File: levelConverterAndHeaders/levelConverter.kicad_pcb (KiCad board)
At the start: 2 copper layers, 30 parts, among them J1 S, J2 Term, J3 S, J4 Term, Q1 BSS138, Q2 BSS138, Q3 BSS138, Q4 BSS138, Q5 BSS138, Q6 BSS138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

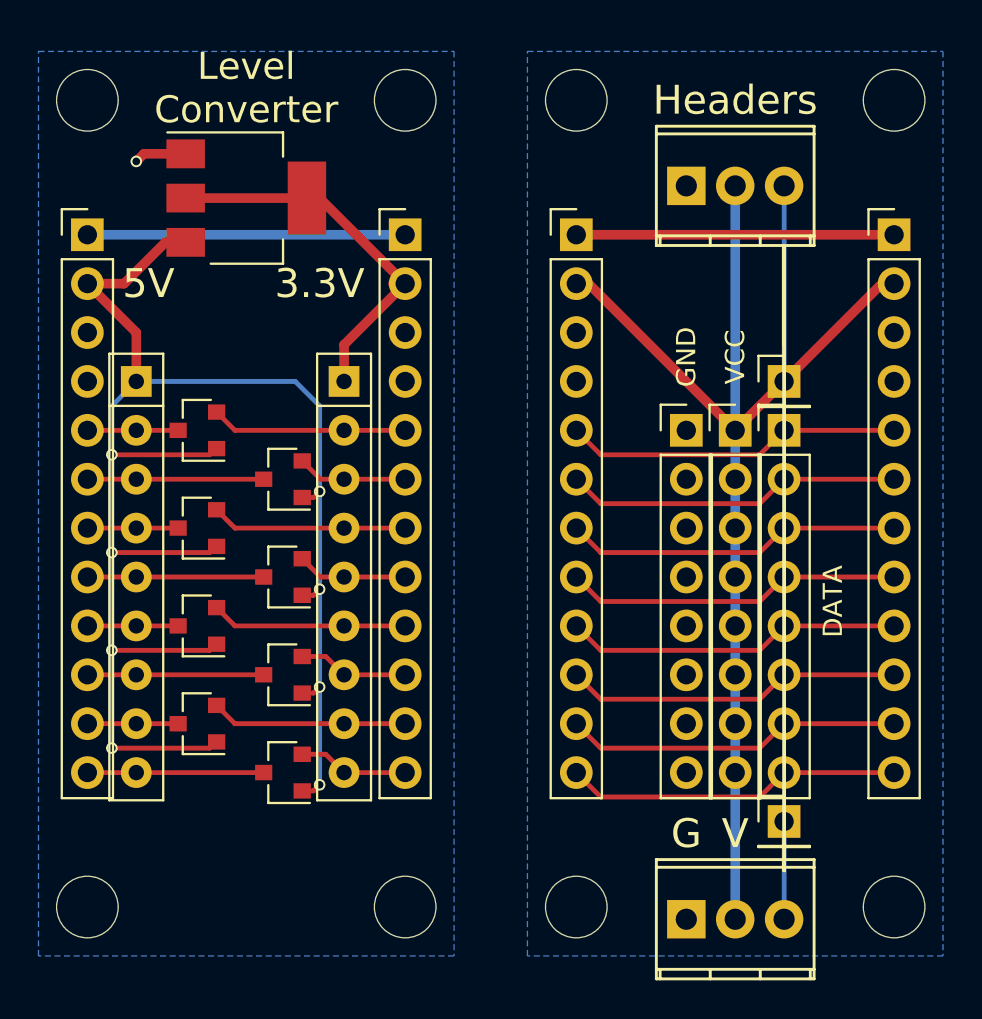
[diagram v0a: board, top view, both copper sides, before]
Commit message: More work to ensure there are no errors from KiCAD's schematic checker. Fixed the multiplexer module, so that all 7 slaves will work (only 6 were working, due to a missing VCC to the "Next Output").
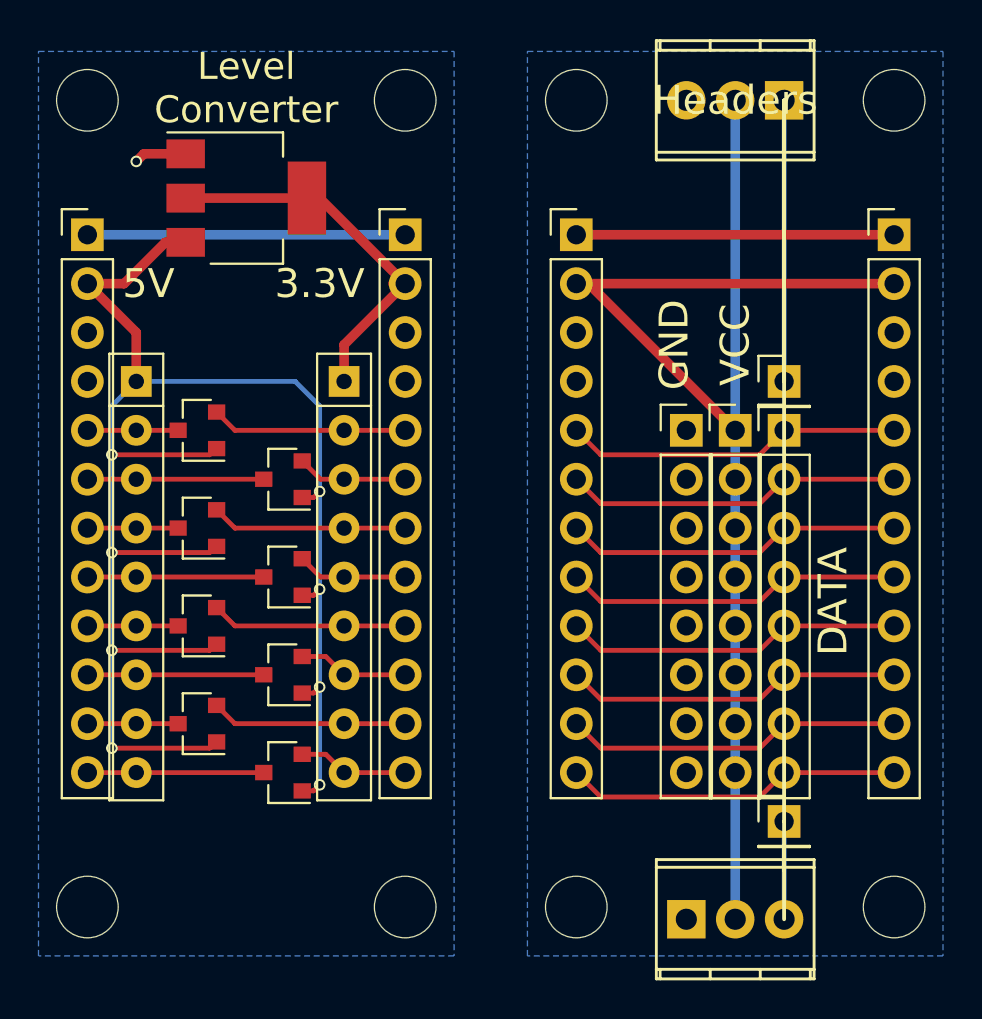
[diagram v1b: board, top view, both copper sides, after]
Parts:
- removed H1: DATA, Pin_Headers:Pin_Header_Straight_1x08_Pitch2.54mm
- removed H2: GND, Pin_Headers:Pin_Header_Straight_1x08_Pitch2.54mm
- removed H3: VCC, Pin_Headers:Pin_Header_Straight_1x08_Pitch2.54mm
- added J5: GND, Pin_Headers:Pin_Header_Straight_1x08_Pitch2.54mm, F.Cu at (159.4, 103.5)
- added J6: VCC, Pin_Headers:Pin_Header_Straight_1x08_Pitch2.54mm, F.Cu at (161.9, 103.5)
- added J7: Data, Pin_Headers:Pin_Header_Straight_1x08_Pitch2.54mm, F.Cu at (164.5, 103.5)
- moved J4 6.75 mm to (164.5, 86.4), turned to 180 degrees
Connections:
- net Net-(H3-Pad1) renamed /VCC2
- I1 pad 3: Earth -> /GND
- I2 pad 3: Earth -> /GND2
- J2 pad 1: Earth -> /GND2
- J4 pad 1: Earth -> Net-(J3-Pad1)
- J4 pad 3: Net-(J3-Pad1) -> /GND2
- O1 pad 3: Earth -> /GND
- O2 pad 3: Earth -> /GND2
- U1 pad 1: Earth -> /GND
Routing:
- net /VCC2: track 60.3 -> 70.5 mm
- net Net-(J3-Pad1): track 10.2 -> 14.6 mm
- net Earth: track 2.73 -> 0.00 mm, vias 1 -> 0
- net /GND: track 0.00 -> 2.73 mm, vias 0 -> 1
- added copper zone on B.Cu, net /GND
- added copper zone on B.Cu, net /GND2
- removed copper zone on B.Cu, net Earth
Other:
- board text added: "DATA"
- board text added: "GND"
- board text added: "VCC"
- board text removed: "G"
- board text removed: "V"
